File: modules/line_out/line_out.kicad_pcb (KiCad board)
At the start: 2 copper layers, 30.5 x 68.6 mm, 19 parts, among them U1 TL072

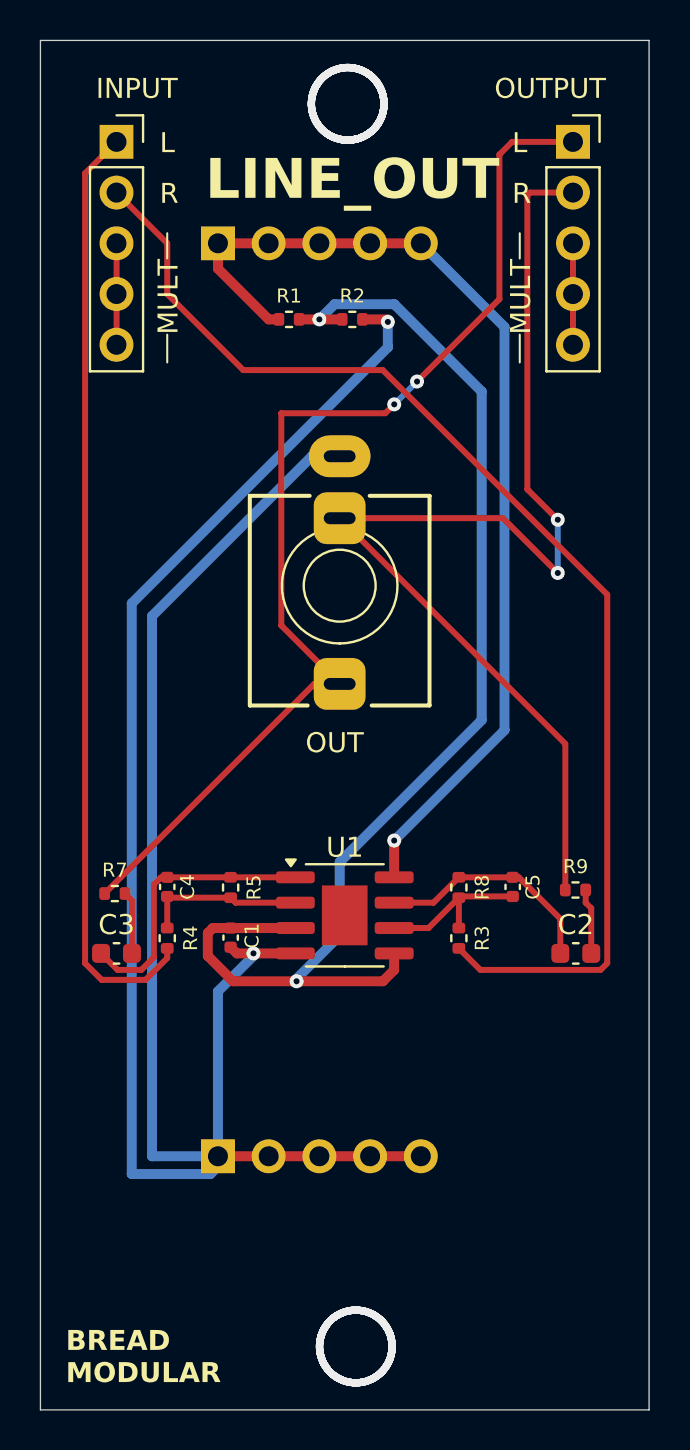
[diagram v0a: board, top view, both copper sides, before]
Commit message: line_out: Introduce input buffering
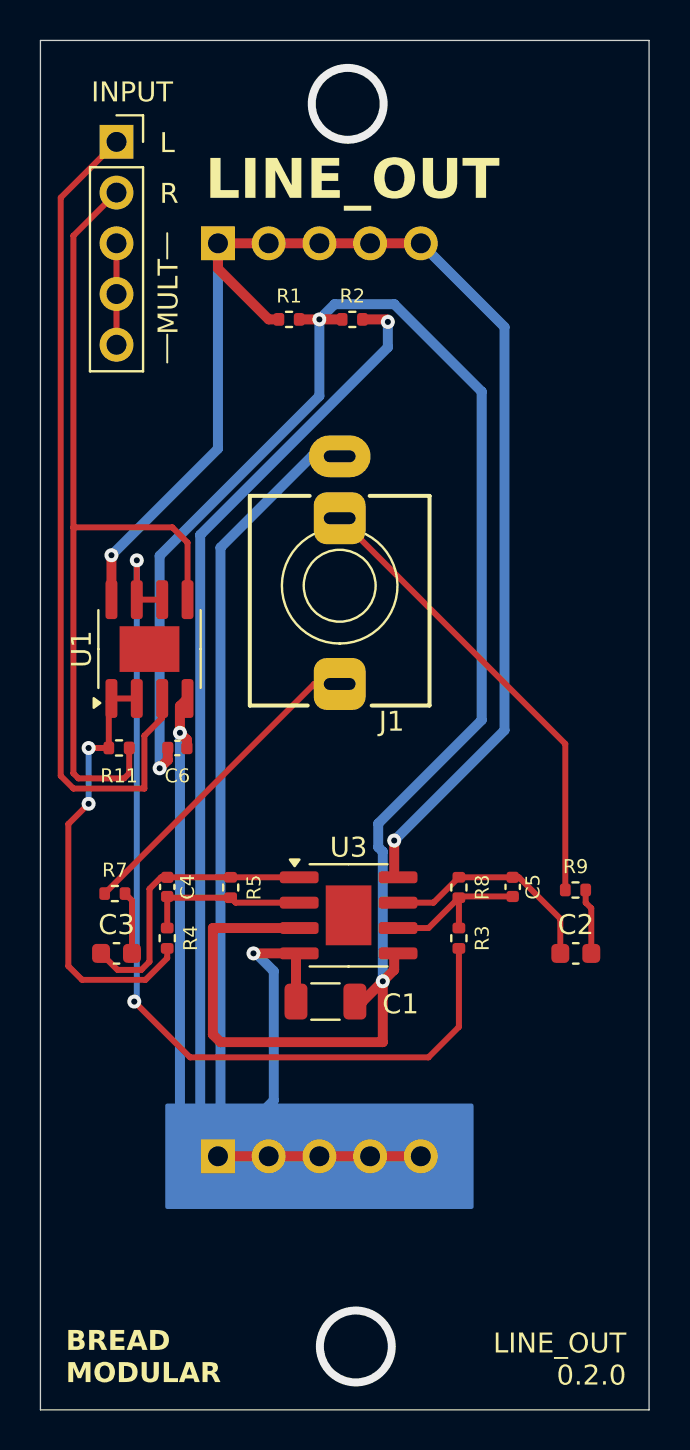
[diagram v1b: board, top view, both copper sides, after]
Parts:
- removed INPUT, OUTPUT: Conn_01x05_Socket, Connector_PinSocket_2.54mm:PinSocket_1x05_P2.54mm_Vertical
- removed OUT: AudioJack3, BreadModular_AudioJacks:Jack_3.5mm_QingPu_WQP-PJ366ST_Vertical
- added C6: 0.1uf, Capacitor_SMD:C_0402_1005Metric, F.Cu at (53.8, 76.1)
- added INPUT1: Conn_01x05_Socket, Connector_PinSocket_2.54mm:PinSocket_1x05_P2.54mm_Vertical, F.Cu at (50.8, 45.7)
- added J1: LineOut, BreadModular_AudioJacks:Jack_3.5mm_QingPu_WQP-PJ366ST_Vertical, F.Cu at (62.0, 67.9)
- added R11: 1M, Resistor_SMD:R_0402_1005Metric, F.Cu at (50.9, 76.1)
- added U3: MCP6002-xSN, Package_SO:SOIC-8-1EP_3.9x4.9mm_P1.27mm_EP2.29x3mm, F.Cu at (62.4, 84.5)
- C1: value 0.1uf -> 100uf; footprint Capacitor_SMD:C_0402_1005Metric -> Capacitor_SMD:C_1206_3216Metric
- C2, C3: value 2.2uf -> 4.7uf
- U1: value TL072 -> MCP6002-xSN
- moved U1 16.5 mm to (52.5, 71.1), turned to 90 degrees
- moved C1 5.73 mm to (61.3, 88.8), turned to 0 degrees
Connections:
- net +5V renamed V_SUPPLY
- C4 pad 2: Net-(U1A--) -> Net-(U3A--)
- C5 pad 2: Net-(U1B--) -> Net-(U3B--)
- R3 pad 1: Net-(U1B--) -> Net-(U3B--)
- R3 pad 2: IN_R -> Net-(U1B--)
- R4 pad 1: Net-(U1A--) -> Net-(U3A--)
- R4 pad 2: IN_L -> Net-(U1A--)
- R5 pad 2: Net-(U1A--) -> Net-(U3A--)
- R8 pad 2: Net-(U1B--) -> Net-(U3B--)
- U1 pad 1: Net-(C3-Pad1) -> Net-(U1A--)
- U1 pad 3: +2.5V -> IN_L
- U1 pad 5: +2.5V -> IN_R
- U1 pad 7: Net-(C2-Pad1) -> Net-(U1B--)
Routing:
- net Net-(U1B--): track 8.11 -> 47.4 mm, vias 0 -> 2
- net OUT_L: track 55.4 -> 16.1 mm, vias 2 -> 0
- net OUT_R: track 57.3 -> 23.3 mm, vias 2 -> 0
- net +2.5V: track 62.4 -> 95.8 mm, vias 2 -> 3
- net GND: track 121.9 -> 145.5 mm, vias 2 -> 3
- net V_SUPPLY: track 51.3 -> 71.4 mm, vias 1 -> 2
- net IN_R: track 60.9 -> 43.1 mm
- net Net-(U1A--): track 8.12 -> 22.3 mm, vias 0 -> 2
- net Net-(U3A--): track 0.00 -> 8.12 mm
- net Net-(U3B--): track 0.00 -> 8.11 mm
- net Net-(OUTPUT2-Pin_3): track 5.08 -> 0.00 mm
- net IN_L: track 47.2 -> 42.2 mm
- net (no net): vias 8 -> 2
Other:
- board text added: "INPUT"
- board text added: "LINE_OUT 0.2.0"

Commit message: Remove opamp for buffering. It adds noise & hums due to use of non-inverting buffers When used inverting buffers L->R relaying has a phase shift So better not to use
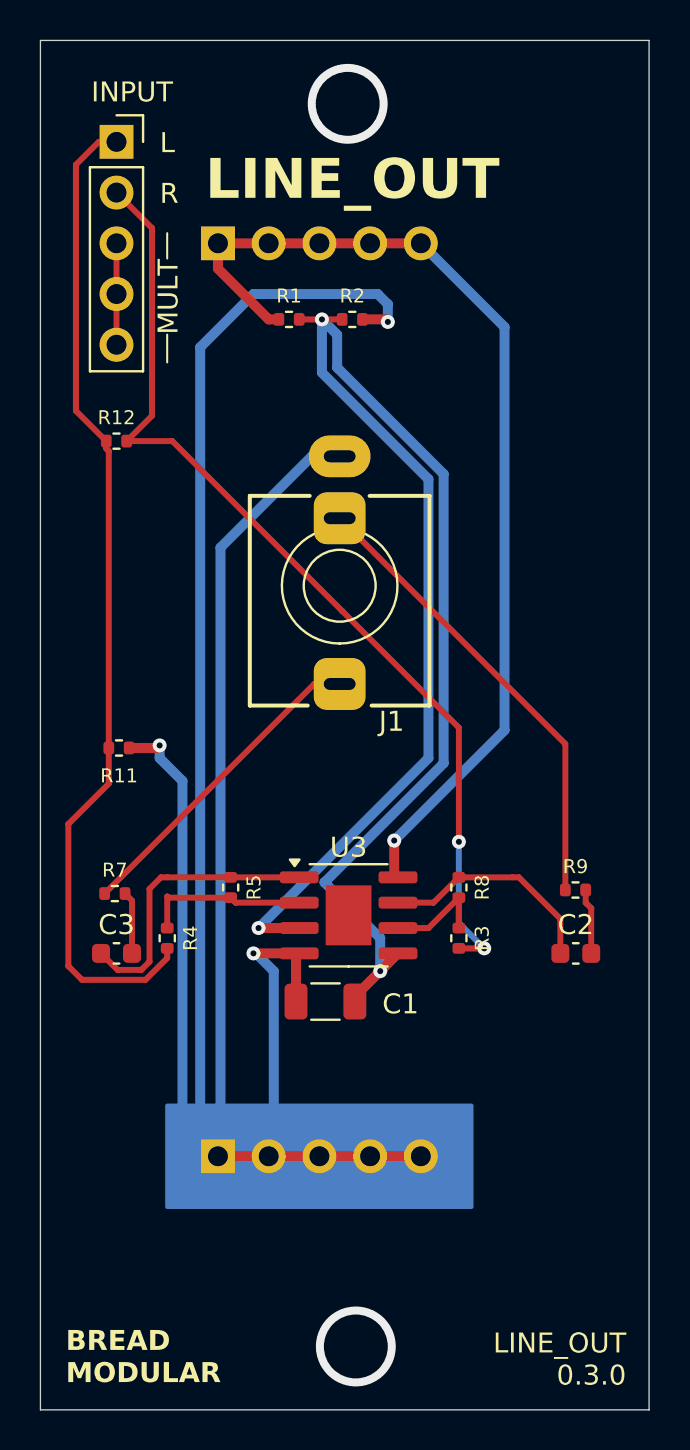
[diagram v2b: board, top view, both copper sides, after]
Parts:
- removed C4, C5: 100pf, Capacitor_SMD:C_0402_1005Metric
- removed C6: 0.1uf, Capacitor_SMD:C_0402_1005Metric
- removed U1: MCP6002-xSN, Package_SO:SOIC-8-1EP_3.9x4.9mm_P1.27mm_EP2.29x3mm
- added R12: 10k, Resistor_SMD:R_0402_1005Metric, F.Cu at (50.8, 60.7)
- R11: value 1M -> 10k
- R3, R4: value 100k -> 1M
- R5, R8: value 33k -> 330k
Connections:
- R11 pad 1: Net-(U1A--) -> IN_L
- R11 pad 2: IN_R -> GND
- R3 pad 2: Net-(U1B--) -> IN_R
- R4 pad 2: Net-(U1A--) -> IN_L
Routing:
- net Net-(U1B--): track 47.4 -> 0.00 mm, vias 2 -> 0
- net Net-(U1A--): track 22.3 -> 0.00 mm, vias 2 -> 0
- net V_SUPPLY: track 71.4 -> 51.3 mm, vias 2 -> 1
- net +2.5V: track 95.8 -> 82.5 mm
- net IN_L: track 42.2 -> 50.3 mm
- net IN_R: track 43.1 -> 49.1 mm, vias 0 -> 2
- net Net-(U3B--): track 8.11 -> 5.47 mm
- net GND: track 145.5 -> 148.0 mm
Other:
- board text added: "LINE_OUT 0.3.0"
- board text removed: "LINE_OUT 0.2.0"

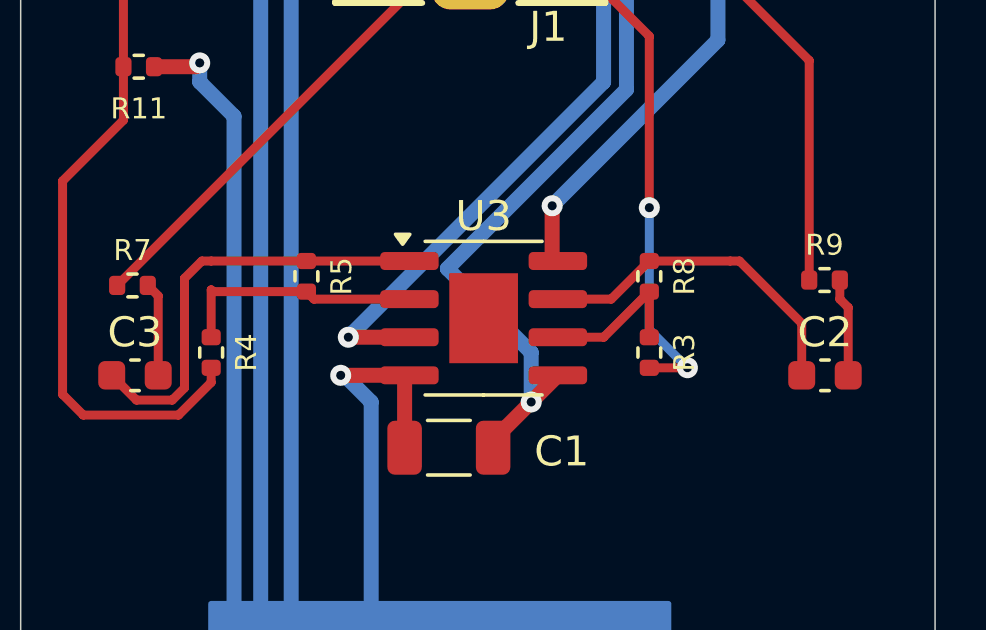
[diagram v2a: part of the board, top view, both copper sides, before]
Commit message: line_out: Update resistor footprints to match with the JLCPCB basic parts
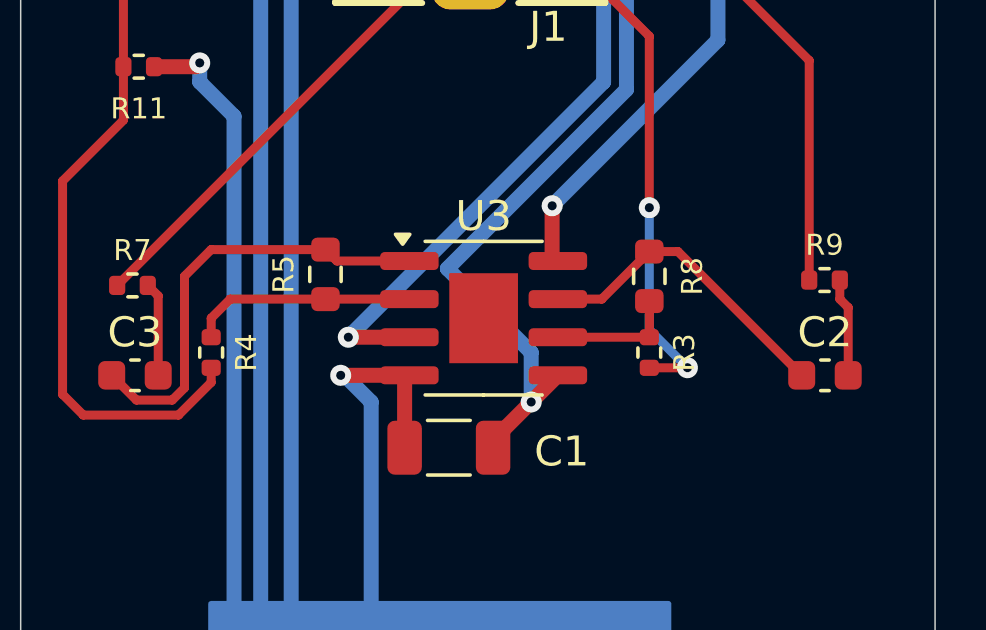
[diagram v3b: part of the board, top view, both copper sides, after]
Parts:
- R5, R8: footprint Resistor_SMD:R_0402_1005Metric -> Resistor_SMD:R_0603_1608Metric
- moved R5 0.64 mm to (57.1, 83.0)
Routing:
- net Net-(U3B--): track 5.47 -> 4.25 mm
- net Net-(C2-Pad1): track 11.4 -> 10.5 mm
- net Net-(U3A--): track 8.12 -> 7.51 mm
- net Net-(C3-Pad1): track 14.1 -> 14.7 mm

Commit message: line_out_1.0.0
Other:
- board text added: "LINE_OUT 1.0.0"
- board text removed: "LINE_OUT 0.3.0"
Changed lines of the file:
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@@
 		)
 	)
-	(gr_text "LINE_OUT\n0.3.0"
+	(gr_text "LINE_OUT\n1.0.0"
 		(at 76.327 108.077 0)
 		(layer "F.SilkS")
